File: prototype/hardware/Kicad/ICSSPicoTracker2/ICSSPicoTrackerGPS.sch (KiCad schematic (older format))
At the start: 0 parts

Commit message: Updated Scehematics and Footprints
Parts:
- added ANT1: Johanson1575, ICSSPicoTracker2:Johanson1575, symbol ICSSPicoTracker:Johanson1575
- added C62, C63, C64, C65, C69, C70, C71: 1uF, Capacitor_SMD:C_0603_1608Metric, symbol Device:C_Small
- added C66: 2.2uF, Capacitor_SMD:C_0603_1608Metric, symbol Device:C_Small
- added C67, C73: 47pF, Capacitor_SMD:C_0402_1005Metric, symbol Device:C_Small
- added C68: 2.7pF, Capacitor_SMD:C_0402_1005Metric, symbol Device:C_Small
- added C72: 1nF, Capacitor_SMD:C_0402_1005Metric, symbol Device:C_Small
- added C74: 100nF, Capacitor_SMD:C_0603_1608Metric, symbol Device:C_Small
- added L20: 8.2nH, Inductor_SMD:L_0402_1005Metric, symbol Device:L_Small
- added L21: 6.8nH, Inductor_SMD:L_0402_1005Metric, symbol Device:L_Small
- added L22: L_Core_Ferrite, Inductor_SMD:L_0603_1608Metric, symbol Device:L_Core_Ferrite
- added R6: 47k, Resistor_SMD:R_0603_1608Metric, symbol Device:R_Small
- added U12: MAX2659ELT+, ICSSPicoTracker2:uDFN-6_1.0x1.5mm_P0.5mm, symbol ICSSPicoTracker:MAX2659ELT+
- added U13: SAFEB1G57KE0F00, ICSSPicoTracker2:Murata SAFE, symbol ICSSPicoTracker:SAFEB1G57KE0F00
- added U14: M8030KT, Package_DFN_QFN:QFN-40-1EP_5x5mm_P0.4mm_EP3.6x3.6mm_ThermalVias, symbol ICSSPicoTracker:M8030KT
- added U15: W25Q16DW, Package_SON:WSON-8-1EP_6x5mm_P1.27mm_EP3.4x4.3mm, symbol ICSSPicoTracker:W25Q16DW
- added X1: 26.00MHz, Oscillator:Oscillator_SMD_SeikoEpson_SG210-4Pin_2.5x2.0mm, symbol Oscillator:IQXO-70
- added Y1: 32.768KHz, Crystal:Crystal_SMD_2012-2Pin_2.0x1.2mm, symbol Device:Crystal
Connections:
- new net: C65.2, L22.2, U14.1 (VDD_ANA), U14.39 (VDD_LNA)
- new net: U14.11 (RTC_O), Y1.1
- new net: U14.12 (RTC_I), Y1.2
- new net: C71.2, U14.2 (LDO_X_OUT), X1.4 (V+)
- new net: C69.2, U14.24 (LDO_C_OUT)
- new net: U14.25 (PIO0), U15.5 (IO_0)
- new net: U14.26 (PIO4), U15.6 (CLK)
- new net: U14.27 (PIO2), U15.3 (IO_2)
- new net: U14.28 (PIO1), U15.2 (IO_1)
- new net: U14.29 (PIO5), U15.1 (CS_N)
- new net: U14.3 (XTAL_I), X1.3 (OUT)
- new net: U14.30 (PIO3), U15.7 (IO_3)
- new net: R6.1, U12.5 (SHDN), U14.37 (PIO16)
- new net: C62.2, L22.1, U14.38 (LDO_RF_OUT)
- new net: L20.2, U14.40 (LNA_IN)
- new net: C66.2, U14.5 (LDO_B_OUT)
- new net: L21.1, U12.3 (RF_IN)
- new net: U12.6 (RF_OUT), U13.1 (RF_IN)
- new net: C67.2, U13.4 (RF_OUT)
- new net: C67.1, C68.2, L20.1
- new net: ANT1.1 (RF_IN), C72.1
- new net: C72.2, L21.2
- new net +1V8: C63.2, C70.1, C73.2, C74.2, U12.4 (VCC), U14.21 (V_DCDC_IN), U14.22 (V_DCDC_OUT), U14.23 (V_CORE), U14.7 (VDD_IO), U15.8 (VCC)
- new net GND: C62.1, C63.1, C64.1, C65.1, C66.1, C68.1, C69.1, C70.2, C71.1, C73.1, C74.1, R6.2, U12.1 (GND), U12.2 (GND), U13.2 (GND), U13.3 (GND), U13.5 (GND), U14.41 (GND), U14.9 (USB_VDD), U15.4 (GND), X1.2 (GND)
- new net GPS_1PPS: U14.35 (PIO11)
- new net GPS_NRES: U14.17 (RESET_N)
- new net GPS_NSAFEBOOT: U14.34 (PIO12)
- new net GPS_RXD: U14.19 (PIO6)
- new net GPS_SCL: U14.31 (PIO8)
- new net GPS_SDA: U14.32 (PIO9)
- new net GPS_TXD: U14.18 (PIO7)
- new net VMEM: C64.2, U14.6 (V_BCKP)
- no-connect marks 0 -> 11

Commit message: Smaller Antenna and try some layouts
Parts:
- X1: footprint Oscillator:Oscillator_SMD_SeikoEpson_SG210-4Pin_2.5x2.0mm -> Oscillator:Oscillator_SMD_IQD_IQXO70-4Pin_7.5x5.0mm
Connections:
- net at U14.37 (PIO16): now also R6.1, U12.5 (SHDN)
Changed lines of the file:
@@
 F 0 "X1" H 2100 3700 50  0000 L CNN
 F 1 "26.00MHz" H 2300 3600 50  0000 L CNN
-F 2 "Oscillator:Oscillator_SMD_SeikoEpson_SG210-4Pin_2.5x2.0mm" H 2725 3125 50  0001 C CNN
+F 2 "Oscillator:Oscillator_SMD_IQD_IQXO70-4Pin_7.5x5.0mm" H 2725 3125 50  0001 C CNN
 F 3 "http://www.iqdfrequencyproducts.com/products/details/iqxo-70-11-30.pdf" H 1950 3450 50  0001 C CNN
 	1    2050 3450
@@
 U 1 1 5D521711
 P 1400 1500
+AR Path="/5D521711" Ref="ANT1"  Part="1"
+AR Path="/5D2ABE03/5D521711" Ref="ANT1"  Part="1"
 F 0 "ANT1" H 1350 1765 50  0000 C CNN
 F 1 "Johanson1575" H 1350 1674 50  0000 C CNN

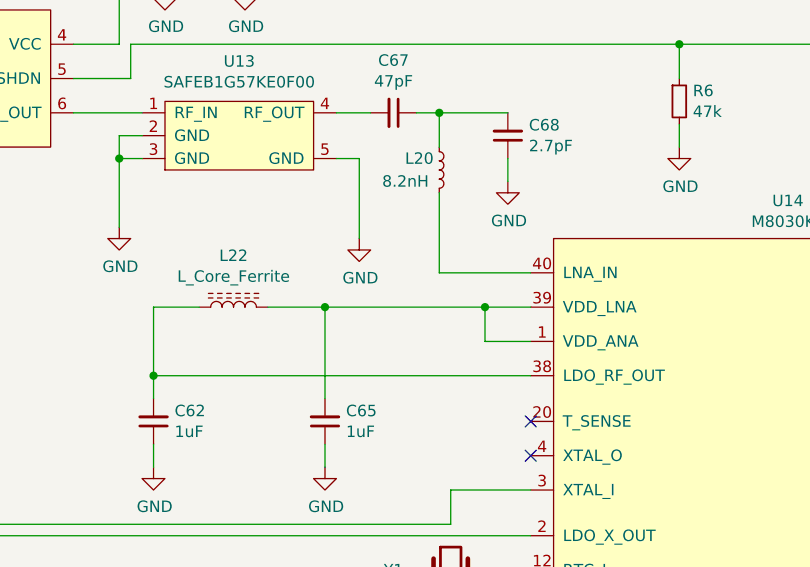
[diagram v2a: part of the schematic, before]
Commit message: Some more ERC fixes
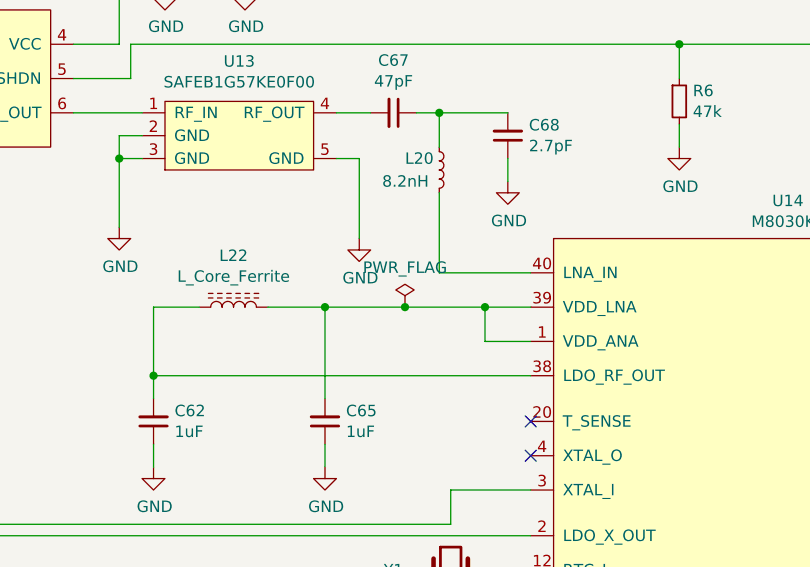
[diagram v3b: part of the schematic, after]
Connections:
- net at U14.37 (PIO16): now also R6.1, U12.5 (SHDN)
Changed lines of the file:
@@
 	4100 3450 4100 3050
 Wire Wire Line
-	4100 3050 4800 3050
+	4100 3050 4450 3050
 Wire Wire Line
 	5000 3850 4650 3850
@@
 Wire Wire Line
 	1900 1500 1800 1500
+$Comp
+L power:PWR_FLAG #FLG0105
+U 1 1 5D648CF0
+P 4450 3050
+F 0 "#FLG0105" H 4450 3125 50  0001 C CNN
+F 1 "PWR_FLAG" H 4450 3223 50  0000 C CNN
+F 2 "" H 4450 3050 50  0001 C CNN
+F 3 "~" H 4450 3050 50  0001 C CNN
+	1    4450 3050
+	1    0    0    -1
+$EndComp
+Connection ~ 4450 3050
+Wire Wire Line
+	4450 3050 4800 3050
 $EndSCHEMATC

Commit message: fully wired up the LD3985 LDO
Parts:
- U14: symbol ICSSPicoTracker:M8030KT -> ICSSPicoTracker2-rescue:M8030KT-ICSSPicoTracker-ICSSPicoTracker2-rescue
- U15: symbol ICSSPicoTracker:W25Q16DW -> ICSSPicoTracker2-rescue:W25Q16DW-ICSSPicoTracker-ICSSPicoTracker2-rescue
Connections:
- net at U14.37 (PIO16): now also R6.1, U12.5 (SHDN)
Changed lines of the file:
@@
 $EndDescr
 $Comp
-L ICSSPicoTracker:W25Q16DW U15
+L ICSSPicoTracker2-rescue:W25Q16DW-ICSSPicoTracker-ICSSPicoTracker2-rescue U15
 U 1 1 5D44A3B3
 P 8900 3750
@@
 NoConn ~ 7250 4850
 $Comp
-L ICSSPicoTracker:M8030KT U14
+L ICSSPicoTracker2-rescue:M8030KT-ICSSPicoTracker-ICSSPicoTracker2-rescue U14
 U 1 1 5D44842F
 P 5100 5800

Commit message: Revert "fully wired up the LD3985 LDO"
This reverts commit 04a440f3a08b8c97db9d4cc44cd5207f890db50a.
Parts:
- U14: symbol ICSSPicoTracker2-rescue:M8030KT-ICSSPicoTracker-ICSSPicoTracker2-rescue -> ICSSPicoTracker:M8030KT
- U15: symbol ICSSPicoTracker2-rescue:W25Q16DW-ICSSPicoTracker-ICSSPicoTracker2-rescue -> ICSSPicoTracker:W25Q16DW
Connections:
- net at U14.37 (PIO16): now also R6.1, U12.5 (SHDN)
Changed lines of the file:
@@
 $EndDescr
 $Comp
-L ICSSPicoTracker2-rescue:W25Q16DW-ICSSPicoTracker-ICSSPicoTracker2-rescue U15
+L ICSSPicoTracker:W25Q16DW U15
 U 1 1 5D44A3B3
 P 8900 3750
@@
 NoConn ~ 7250 4850
 $Comp
-L ICSSPicoTracker2-rescue:M8030KT-ICSSPicoTracker-ICSSPicoTracker2-rescue U14
+L ICSSPicoTracker:M8030KT U14
 U 1 1 5D44842F
 P 5100 5800
